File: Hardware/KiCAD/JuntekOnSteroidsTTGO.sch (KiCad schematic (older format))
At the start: 34 parts, among them J1 To PSU host board, J11 patch, J12 patch, J2 To PSU host board, J21 patch, J22 patch, J23 patch, J30 Expansion1, J4 ESP32-TFT, J5 ESP32-TFT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

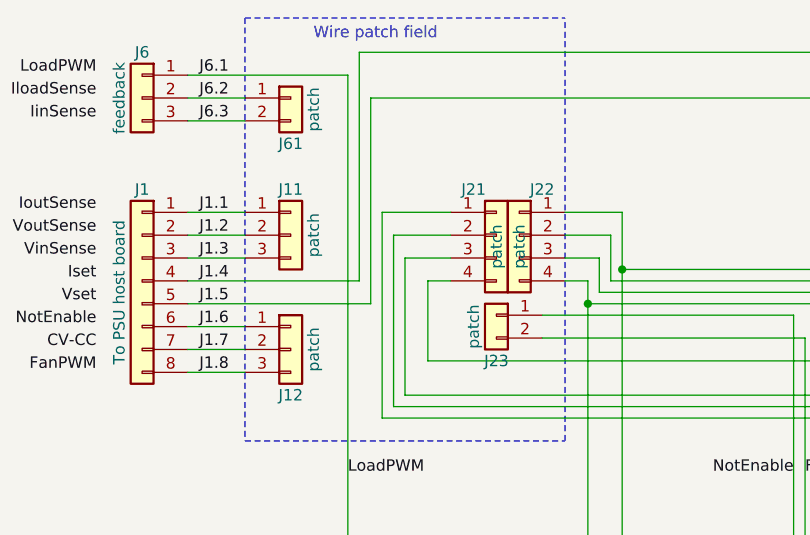
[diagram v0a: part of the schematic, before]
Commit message: 90-deg patch headers
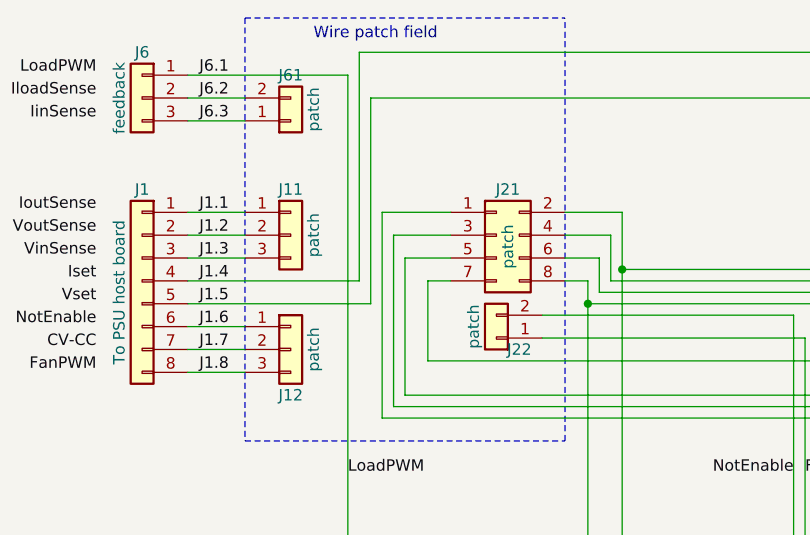
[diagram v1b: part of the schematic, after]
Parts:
- removed J21, J22: patch, Connector_PinHeader_2.54mm:PinHeader_1x04_P2.54mm_Vertical, symbol Connector_Generic:Conn_01x04
- added J21: patch, Connector_PinHeader_2.54mm:PinHeader_2x04_P2.54mm_Horizontal, symbol Connector_Generic:Conn_02x04_Odd_Even
- J11, J12: footprint Connector_PinHeader_2.54mm:PinHeader_1x03_P2.54mm_Vertical -> Connector_PinHeader_2.54mm:PinHeader_1x03_P2.54mm_Horizontal
- J22: renamed from J23; footprint Connector_PinHeader_2.54mm:PinHeader_1x02_P2.54mm_Vertical -> Connector_PinHeader_2.54mm:PinHeader_1x02_P2.54mm_Horizontal
- J61: footprint Connector_PinHeader_2.54mm:PinHeader_1x02_P2.54mm_Vertical -> Connector_PinHeader_2.54mm:PinHeader_1x02_P2.54mm_Horizontal
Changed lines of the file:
@@
 Wire Wire Line
 	4050 5700 4250 5700
-$Comp
-L Connector_Generic:Conn_01x02 J23
-U 1 1 618B9DDF
-P 3500 3950
-F 0 "J23" H 3500 3750 50  0000 C CNN
-F 1 "patch" V 3600 3900 50  0000 C CNN
-F 2 "Connector_PinHeader_2.54mm:PinHeader_1x02_P2.54mm_Vertical" H 3500 3950 50  0001 C CNN
-F 3 "~" H 3500 3950 50  0001 C CNN
-	1    3500 3950
-	-1   0    0    -1
-$EndComp
-$Comp
-L Connector_Generic:Conn_01x04 J21
-U 1 1 618C97C3
-P 3500 3600
-F 0 "J21" H 3400 3800 50  0000 C CNN
-F 1 "patch" V 3500 3550 50  0000 C CNN
-F 2 "Connector_PinHeader_2.54mm:PinHeader_1x04_P2.54mm_Vertical" H 3500 3600 50  0001 C CNN
-F 3 "~" H 3500 3600 50  0001 C CNN
-	1    3500 3600
-	1    0    0    -1
-$EndComp
 Wire Wire Line
 	10050 4600 10200 4600
 Wire Wire Line
 	10050 4800 10250 4800
-$Comp
-L Connector_Generic:Conn_01x04 J22
-U 1 1 61903835
-P 3600 3600
-F 0 "J22" H 3500 3800 50  0000 C CNN
-F 1 "patch" V 3600 3550 50  0000 C CNN
-F 2 "Connector_PinHeader_2.54mm:PinHeader_1x04_P2.54mm_Vertical" H 3600 3600 50  0001 C CNN
-F 3 "~" H 3600 3600 50  0001 C CNN
-	1    3600 3600
-	-1   0    0    -1
-$EndComp
 Wire Wire Line
 	4050 3500 4050 3750
@@
 F 0 "J11" H 2600 3800 50  0000 C CNN
 F 1 "patch" V 2700 3600 50  0000 C CNN
-F 2 "Connector_PinHeader_2.54mm:PinHeader_1x03_P2.54mm_Vertical" H 2600 3600 50  0001 C CNN
+F 2 "Connector_PinHeader_2.54mm:PinHeader_1x03_P2.54mm_Horizontal" H 2600 3600 50  0001 C CNN
 F 3 "~" H 2600 3600 50  0001 C CNN
 	1    2600 3600
@@
 L Connector_Generic:Conn_01x02 J61
 U 1 1 61BF9BF7
-P 2600 3000
-F 0 "J61" H 2600 2800 50  0000 C CNN
-F 1 "patch" V 2700 2950 50  0000 C CNN
-F 2 "Connector_PinHeader_2.54mm:PinHeader_1x02_P2.54mm_Vertical" H 2600 3000 50  0001 C CNN
-F 3 "~" H 2600 3000 50  0001 C CNN
-	1    2600 3000
-	1    0    0    -1
+P 2600 3100
+F 0 "J61" H 2600 2900 50  0000 C CNN
+F 1 "patch" V 2700 3050 50  0000 C CNN
+F 2 "Connector_PinHeader_2.54mm:PinHeader_1x02_P2.54mm_Horizontal" H 2600 3100 50  0001 C CNN
+F 3 "~" H 2600 3100 50  0001 C CNN
+	1    2600 3100
+	1    0    0    1
 $EndComp
 $Comp
@@
 F 0 "J12" H 2600 3900 50  0000 C CNN
 F 1 "patch" V 2700 4100 50  0000 C CNN
-F 2 "Connector_PinHeader_2.54mm:PinHeader_1x03_P2.54mm_Vertical" H 2600 4100 50  0001 C CNN
+F 2 "Connector_PinHeader_2.54mm:PinHeader_1x03_P2.54mm_Horizontal" H 2600 4100 50  0001 C CNN
 F 3 "~" H 2600 4100 50  0001 C CNN
 	1    2600 4100
@@
 	9900 5050 10150 5050
 Connection ~ 10150 5050
+$Comp
+L Connector_Generic:Conn_01x02 J22
+U 1 1 618B9DDF
+P 3500 4050
+F 0 "J22" H 3400 4100 50  0000 C CNN
+F 1 "patch" V 3600 4000 50  0000 C CNN
+F 2 "Connector_PinHeader_2.54mm:PinHeader_1x02_P2.54mm_Horizontal" H 3500 4050 50  0001 C CNN
+F 3 "~" H 3500 4050 50  0001 C CNN
+	1    3500 4050
+	-1   0    0    1
+$EndComp
+$Comp
+L Connector_Generic:Conn_02x04_Odd_Even J21
+U 1 1 61296448
+P 3500 3600
+F 0 "J21" H 3550 3800 50  0000 C CNN
+F 1 "patch" V 3550 3550 50  0000 C CNN
+F 2 "Connector_PinHeader_2.54mm:PinHeader_2x04_P2.54mm_Horizontal" H 3500 3600 50  0001 C CNN
+F 3 "~" H 3500 3600 50  0001 C CNN
+	1    3500 3600
+	1    0    0    -1
+$EndComp
 $EndSCHEMATC

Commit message: routed
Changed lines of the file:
@@
 Sheet 1 1
 Title "Drok/Juntek-on-steroids"
-Date "2021-08-19"
-Rev "2.3"
+Date "2021-08-21"
+Rev "2.4"
 Comp ""
 Comment1 ""
@@
 	9450 4000 9850 4000
 Connection ~ 9450 4000
-Text Label 9150 5500 1    50   ~ 0
+Text Label 8450 5600 1    50   ~ 0
 SDA
-Text Label 9050 5500 1    50   ~ 0
+Text Label 8550 5600 1    50   ~ 0
 SCL
-Text Label 8850 5500 1    50   ~ 0
+Text Label 8750 5600 1    50   ~ 0
 GPIO13
-Text Label 8950 5500 1    50   ~ 0
+Text Label 8650 5600 1    50   ~ 0
 GPIO17
-Text Label 9350 5500 1    50   ~ 0
-GND
-Text Label 8350 5500 1    50   ~ 0
+Text Label 8250 5600 1    50   ~ 0
 GND
 Text Label 2200 3500 0    50   ~ 0
@@
 Text Label 1750 3900 2    50   ~ 0
 Vset
-Text Label 8750 5500 1    50   ~ 0
+Text Label 8950 5600 1    50   ~ 0
 GPIO12
-Text Label 8650 5500 1    50   ~ 0
+Text Label 9050 5600 1    50   ~ 0
 GPIO25
-Text Label 8550 5500 1    50   ~ 0
+Text Label 9150 5600 1    50   ~ 0
 GPIO26
-Text Label 8450 5500 1    50   ~ 0
+Text Label 9250 5600 1    50   ~ 0
 GPIO27
-Text Label 9250 5500 1    50   ~ 0
+Text Label 8350 5600 1    50   ~ 0
 +3V3
-Text Label 8250 5500 1    50   ~ 0
+Text Label 9350 5600 1    50   ~ 0
 +5V
 Wire Wire Line
@@
 Text Label 1750 3000 2    50   ~ 0
 IloadSense
-Wire Wire Line
-	9350 5500 9350 5550
-Wire Wire Line
-	9250 5550 9250 5500
-Wire Wire Line
-	9150 5500 9150 5550
-Wire Wire Line
-	9050 5550 9050 5500
-Wire Wire Line
-	8950 5500 8950 5550
-Wire Wire Line
-	8850 5550 8850 5500
-Wire Wire Line
-	8750 5500 8750 5550
-Wire Wire Line
-	8650 5550 8650 5500
-Wire Wire Line
-	8550 5500 8550 5550
-Wire Wire Line
-	8450 5550 8450 5500
-Wire Wire Line
-	8350 5500 8350 5550
-Wire Wire Line
-	8250 5550 8250 5500
 $Comp
 L Device:R R14
@@
 	1    0    0    -1
 $EndComp
+Text Label 8850 5600 1    50   ~ 0
+GPIO2
+Wire Wire Line
+	8250 5600 8250 5700
+Wire Wire Line
+	8350 5600 8350 5700
+Wire Wire Line
+	8450 5600 8450 5700
+Wire Wire Line
+	8550 5600 8550 5700
+Wire Wire Line
+	8650 5600 8650 5700
+Wire Wire Line
+	8750 5600 8750 5700
+Wire Wire Line
+	8850 5600 8850 5700
+Wire Wire Line
+	8950 5600 8950 5700
+Wire Wire Line
+	9050 5600 9050 5700
+Wire Wire Line
+	9150 5600 9150 5700
+Wire Wire Line
+	9250 5600 9250 5700
+Wire Wire Line
+	9350 5600 9350 5700
 $EndSCHEMATC

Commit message: AltVinSense replacing LoadPWM
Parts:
- removed R19: 10k/none, Resistor_THT:R_Axial_DIN0204_L3.6mm_D1.6mm_P7.62mm_Horizontal, symbol Device:R
- added R13: 1k/zero, Resistor_THT:R_Axial_DIN0204_L3.6mm_D1.6mm_P7.62mm_Horizontal, symbol Device:R
- J61: footprint Connector_PinHeader_2.54mm:PinHeader_1x02_P2.54mm_Horizontal -> Connector_PinHeader_2.54mm:PinHeader_1x03_P2.54mm_Horizontal; symbol Connector_Generic:Conn_01x02 -> Connector_Generic:Conn_01x03
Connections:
- net A2: now also R13.2; no longer J21.5 (Pin_5)
- net ADC0: no longer R20.1
- net GPIO12: no longer J6.1 (Pin_1)
- new net: J21.5 (Pin_5), R13.1
- new net J6.1: J6.1 (Pin_1), J61.3 (Pin_3), R20.1
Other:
- moved on the sheet: R20
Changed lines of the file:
@@
 P 5200 4150
 F 0 "R17" V 5200 4150 50  0000 C CNN
-F 1 "1k/zero" V 5300 4150 50  0000 C CNN
+F 1 "1k/zero" V 5250 3900 50  0000 C CNN
 F 2 "Resistor_THT:R_Axial_DIN0204_L3.6mm_D1.6mm_P7.62mm_Horizontal" V 5130 4150 50  0001 C CNN
 F 3 "~" H 5200 4150 50  0001 C CNN
@@
 L Device:R R20
 U 1 1 60BCC05A
-P 4050 5500
-F 0 "R20" V 4050 5500 50  0000 C CNN
-F 1 "100k/none" V 4150 5550 50  0000 C CNN
-F 2 "Resistor_THT:R_Axial_DIN0204_L3.6mm_D1.6mm_P7.62mm_Horizontal" V 3980 5500 50  0001 C CNN
-F 3 "~" H 4050 5500 50  0001 C CNN
-	1    4050 5500
+P 4100 5500
+F 0 "R20" V 4100 5500 50  0000 C CNN
+F 1 "100k/none" V 4200 5550 50  0000 C CNN
+F 2 "Resistor_THT:R_Axial_DIN0204_L3.6mm_D1.6mm_P7.62mm_Horizontal" V 4030 5500 50  0001 C CNN
+F 3 "~" H 4100 5500 50  0001 C CNN
+	1    4100 5500
 	1    0    0    -1
 $EndComp
@@
 Wire Notes Line
 	5900 5900 5900 3100
-Wire Wire Line
-	4250 5650 4250 5700
-Text Label 4250 5700 0    50   ~ 0
+Text Label 4350 5700 0    50   ~ 0
 GND
-$Comp
-L Device:R R19
-U 1 1 61C6481B
-P 4250 5500
-F 0 "R19" V 4250 5500 50  0000 C CNN
-F 1 "10k/none" V 4350 5600 50  0000 C CNN
-F 2 "Resistor_THT:R_Axial_DIN0204_L3.6mm_D1.6mm_P7.62mm_Horizontal" V 4180 5500 50  0001 C CNN
-F 3 "~" H 4250 5500 50  0001 C CNN
-	1    4250 5500
-	1    0    0    -1
-$EndComp
 Wire Wire Line
 	6600 5200 6600 5550
-Wire Wire Line
-	4250 5350 4250 5100
-Connection ~ 4250 5100
 $Comp
 L Device:R R15
@@
 $EndComp
 Wire Wire Line
-	4250 5700 4800 5700
-Wire Wire Line
 	4800 5700 4800 5650
 Wire Wire Line
 	6900 4350 6900 4650
-Wire Wire Line
-	7000 4300 7000 4650
 Wire Wire Line
 	6700 2800 6700 3450
@@
 	6900 5100 6900 5550
 Wire Wire Line
-	4250 5100 6900 5100
-Wire Wire Line
 	6800 5500 6800 5550
 Text Label 1750 2900 2    50   ~ 0
-LoadPWM
+AltVinSense
 Text Label 1750 3000 2    50   ~ 0
 IloadSense
@@
 	-1   0    0    1
 $EndComp
-Connection ~ 4250 5700
-Wire Wire Line
-	4050 5650 4050 5700
+Wire Wire Line
+	4100 5650 4100 5700
 $Comp
 L Device:R R11
@@
 	3050 4350 6900 4350
 Wire Wire Line
-	3100 3700 3100 4300
-Wire Wire Line
-	3100 4300 7000 4300
+	3100 3700 3100 4250
 Wire Wire Line
 	6400 3450 6400 3850
@@
 	7100 4150 7100 4650
 Wire Wire Line
-	4050 3750 4050 5350
-Connection ~ 4050 5700
-Wire Wire Line
-	4050 5700 4250 5700
-Wire Wire Line
 	10050 4600 10200 4600
 Wire Wire Line
@@
 Wire Wire Line
 	4050 3500 4050 3750
-Connection ~ 4050 3750
-Wire Wire Line
-	4050 3750 6200 3750
 Wire Wire Line
 	4000 3600 4000 3800
@@
 Wire Wire Line
 	3900 3900 6500 3900
-Wire Wire Line
-	3900 5700 4050 5700
 Wire Wire Line
 	3200 3800 3300 3800
@@
 	2150 3800 2900 3800
 $Comp
-L Connector_Generic:Conn_01x02 J61
+L Connector_Generic:Conn_01x03 J61
 U 1 1 61BF9BF7
-P 2600 3100
-F 0 "J61" H 2600 2900 50  0000 C CNN
-F 1 "patch" V 2700 3050 50  0000 C CNN
-F 2 "Connector_PinHeader_2.54mm:PinHeader_1x02_P2.54mm_Horizontal" H 2600 3100 50  0001 C CNN
-F 3 "~" H 2600 3100 50  0001 C CNN
-	1    2600 3100
+P 2600 3000
+F 0 "J61" H 2600 2800 50  0000 C CNN
+F 1 "patch" V 2700 2950 50  0000 C CNN
+F 2 "Connector_PinHeader_2.54mm:PinHeader_1x03_P2.54mm_Horizontal" H 2600 3000 50  0001 C CNN
+F 3 "~" H 2600 3000 50  0001 C CNN
+	1    2600 3000
 	1    0    0    1
 $EndComp
@@
 Text Label 4800 4650 2    50   ~ 0
 NotEnable
-Wire Wire Line
-	2850 2900 2850 5100
-Wire Wire Line
-	2850 5100 4250 5100
-Wire Wire Line
-	2150 2900 2850 2900
-Text Label 2850 4650 0    50   ~ 0
+Text Label 6900 5100 0    50   ~ 0
 LoadPWM
 Wire Notes Line
@@
 Wire Wire Line
 	9350 5600 9350 5700
+$Comp
+L Device:R R13
+U 1 1 61232F23
+P 5200 4250
+F 0 "R13" V 5200 4250 50  0000 C CNN
+F 1 "1k/zero" V 5150 4000 50  0000 C CNN
+F 2 "Resistor_THT:R_Axial_DIN0204_L3.6mm_D1.6mm_P7.62mm_Horizontal" V 5130 4250 50  0001 C CNN
+F 3 "~" H 5200 4250 50  0001 C CNN
+	1    5200 4250
+	0    -1   -1   0
+$EndComp
+Wire Wire Line
+	5350 4250 7000 4250
+Wire Wire Line
+	5050 4250 3100 4250
+Wire Wire Line
+	7000 4250 7000 4650
+Wire Wire Line
+	2150 2900 2400 2900
+Wire Wire Line
+	3900 5700 4100 5700
+Wire Wire Line
+	2400 2900 4100 2900
+Connection ~ 2400 2900
+Wire Wire Line
+	4050 3750 6200 3750
+Wire Wire Line
+	4100 2900 4100 5350
+Connection ~ 4100 5700
+Wire Wire Line
+	4100 5700 4800 5700
 $EndSCHEMATC

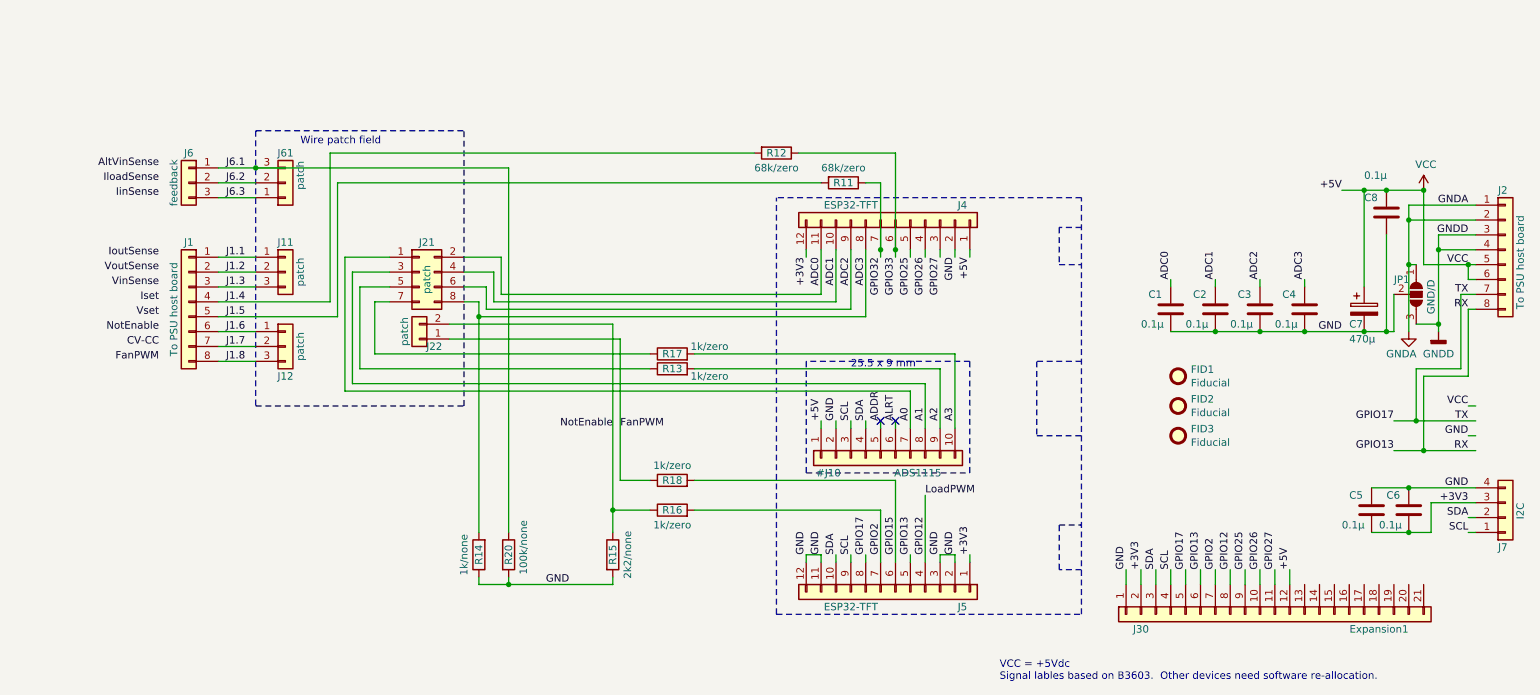
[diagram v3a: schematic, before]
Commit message: Change ADS115 to 3.3V & other tweaks
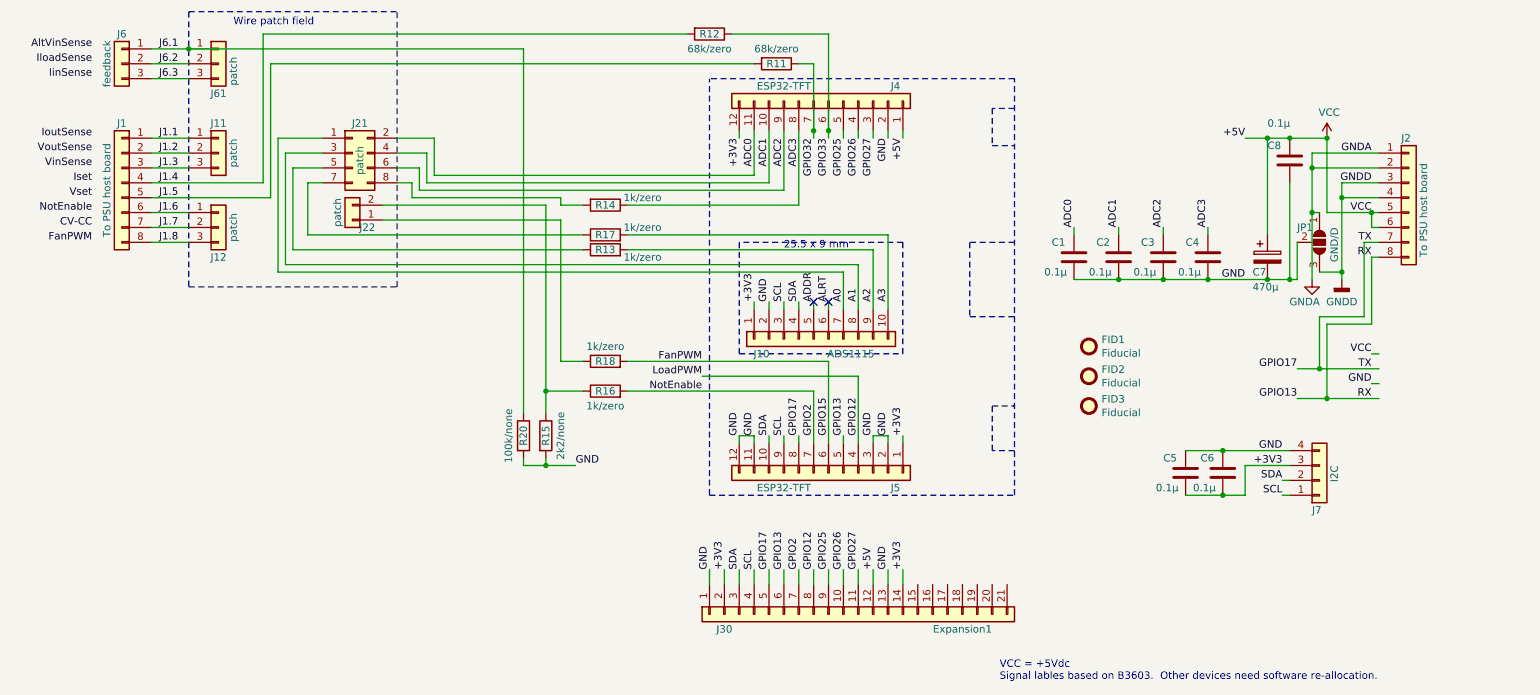
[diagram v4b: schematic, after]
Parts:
- added J10: ADS1115, Connector_PinSocket_2.54mm:PinSocket_1x10_P2.54mm_Vertical, symbol Connector_Generic:Conn_01x10
- R14: value 1k/none -> 1k/zero
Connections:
- net GPIO15 is gone; now on net FanPWM: J5.6 (Pin_6), R18.2
- net +3V3: now also J30.14 (Pin_14), J10.1 (Pin_1)
- net A0: now also J10.7 (Pin_7)
- net A1: now also J10.8 (Pin_8)
- net A2: now also J10.9 (Pin_9)
- net A3: now also J10.10 (Pin_10)
- net ADC3: now also R14.1; no longer J21.8 (Pin_8), R14.2
- net ADDR: now also J10.5 (Pin_5)
- net ALRT: now also J10.6 (Pin_6)
- net FanPWM: no longer J22.1 (Pin_1), R18.1
- net GND: now also J30.13 (Pin_13), J10.2 (Pin_2); no longer R14.1
- net J6.1: now also J61.1 (Pin_1); no longer J61.3 (Pin_3)
- net J6.3: now also J61.3 (Pin_3); no longer J61.1 (Pin_1)
- net SCL: now also J10.3 (Pin_3)
- net SDA: now also J10.4 (Pin_4)
- net NotEnable: no longer names the net of J22.2 (Pin_2), R15.1, R16.1
- new net: J21.8 (Pin_8), R14.2
- new net: J22.1 (Pin_1), R18.1
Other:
- moved on the sheet: C1, C2, C3, C4, C5, C6, C7, C8, FID1, FID2, FID3, J1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
